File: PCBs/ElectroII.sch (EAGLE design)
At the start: 30 parts, among them J1 U.FL-R-SMT(01), U1 RFM95W-868S2, U2 TPS61090RSAR

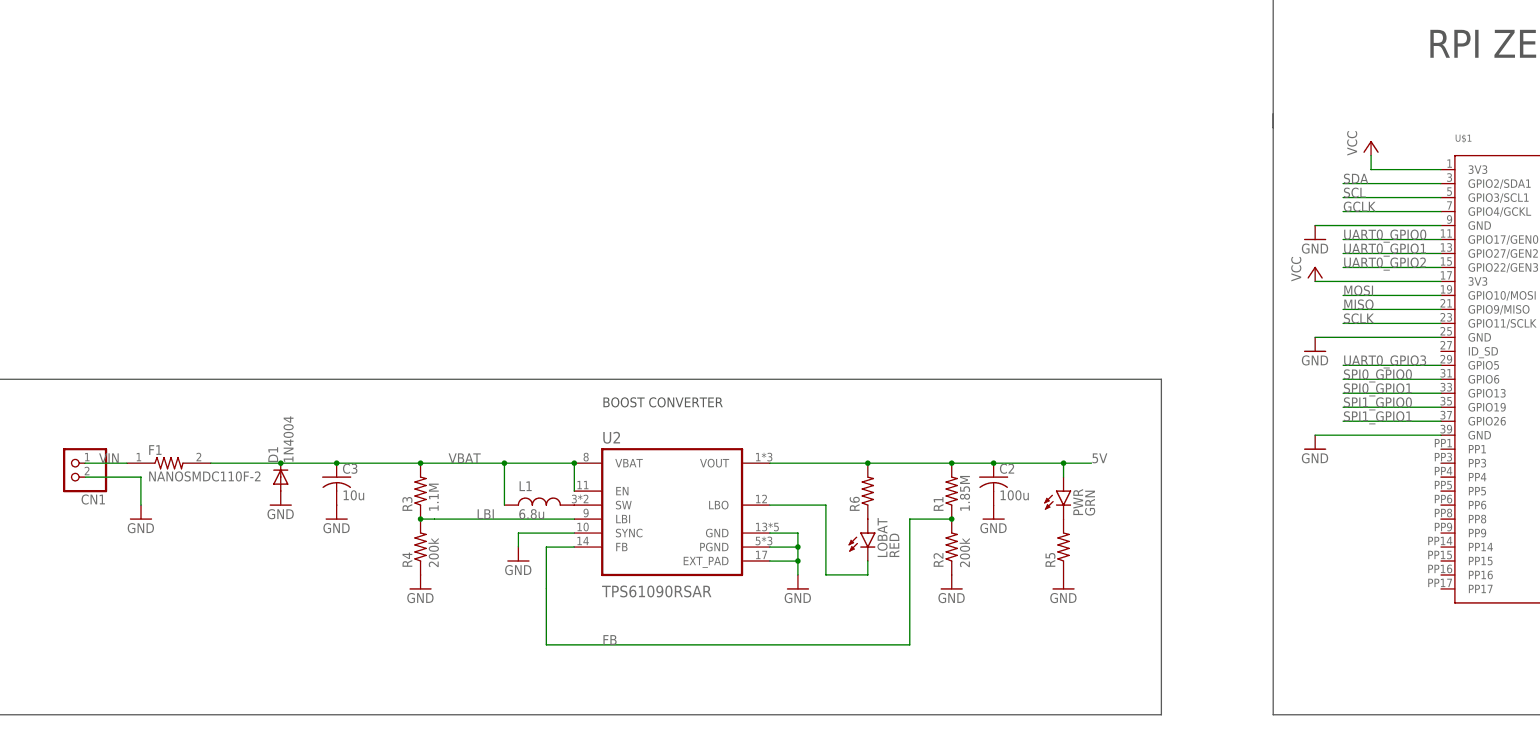
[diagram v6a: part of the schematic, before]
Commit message: Added sample pins and new trace ideas
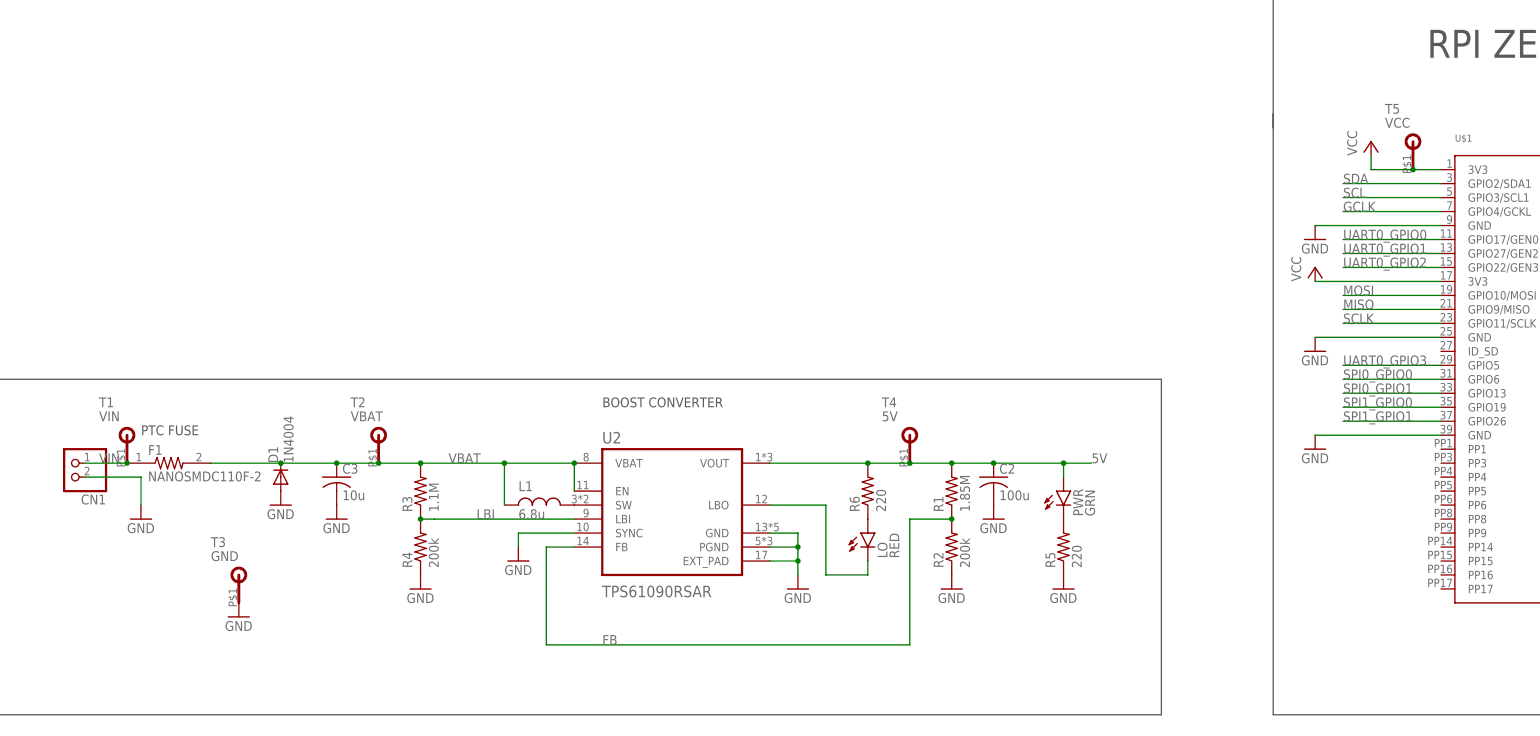
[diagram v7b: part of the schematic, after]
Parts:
- added T1: VIN, RTR Main Library:TEST_PAD
- added T2: VBAT, RTR Main Library:TEST_PAD
- added T3: GND, RTR Main Library:TEST_PAD
- added T4: 5V, RTR Main Library:TEST_PAD
- added T5: VCC, RTR Main Library:TEST_PAD
- R5, R6: value (none) -> 220
- renumbered LOBAT to LO
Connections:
- net 5V: now also T4.P$1
- net GND: now also T3.P$1
- net VBAT: now also T2.P$1
- net VCC: now also T5.P$1
- net VIN: now also T1.P$1
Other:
- note added: "PTC FUSE"
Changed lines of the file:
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@@
 </class>
 <class number="1" name="PWR" width="0.508" drill="0">
-<clearance class="1" value="0.1524"/>
+<clearance class="1" value="0.2032"/>
 </class>
 <class number="2" name="GND" width="0.508" drill="0">
-<clearance class="2" value="0.1524"/>
+<clearance class="2" value="0.2032"/>
+</class>
+<class number="3" name="ANT" width="0.2032" drill="0">
+<clearance class="3" value="0.3048"/>
 </class>
 </classes>
@@
 <part name="R4" library="RTR Main Library" deviceset="R-ALL_PACKAGES" device="R1206" value="200k"/>
 <part name="PWR" library="RTR Main Library" deviceset="LED" device="5MM" package3d_urn="urn:adsk.eagle:package:15799/2" value="GRN"/>
-<part name="R5" library="RTR Main Library" deviceset="R-ALL_PACKAGES" device="R1206"/>
+<part name="R5" library="RTR Main Library" deviceset="R-ALL_PACKAGES" device="R1206" value="220"/>
 <part name="GND22" library="RTR Main Library" deviceset="GND" device=""/>
 <part name="C3" library="RTR Main Library" deviceset="C-ALL_PACKAGES" device="C1206" value="10u"/>
 <part name="GND23" library="RTR Main Library" deviceset="GND" device=""/>
-<part name="LOBAT" library="RTR Main Library" deviceset="LED" device="5MM" package3d_urn="urn:adsk.eagle:package:15799/2" value="RED"/>
-<part name="R6" library="RTR Main Library" deviceset="R-ALL_PACKAGES" device="R1206"/>
+<part name="LO" library="RTR Main Library" deviceset="LED" device="5MM" package3d_urn="urn:adsk.eagle:package:15799/2" value="RED"/>
+<part name="R6" library="RTR Main Library" deviceset="R-ALL_PACKAGES" device="R1206" value="220"/>
 <part name="D1" library="adafruit" library_urn="urn:adsk.eagle:library:420" deviceset="1N4004" device="" package3d_urn="urn:adsk.eagle:package:6240344/1"/>
 <part name="GND24" library="RTR Main Library" deviceset="GND" device=""/>
@@
 <part name="GND25" library="RTR Main Library" deviceset="GND" device=""/>
 <part name="F1" library="NANOSMDC110F-2" deviceset="NANOSMDC110F-2" device=""/>
+<part name="GND26" library="RTR Main Library" deviceset="GND" device=""/>
+<part name="T1" library="RTR Main Library" deviceset="TEST_PAD" device="" value="VIN"/>
+<part name="T2" library="RTR Main Library" deviceset="TEST_PAD" device="" value="VBAT"/>
+<part name="T3" library="RTR Main Library" deviceset="TEST_PAD" device="" value="GND"/>
+<part name="T4" library="RTR Main Library" deviceset="TEST_PAD" device="" value="5V"/>
+<part name="T5" library="RTR Main Library" deviceset="TEST_PAD" device="" value="VCC"/>
 </parts>
 <sheets>
@@
 <wire x1="-322.58" y1="-68.58" x2="-322.58" y2="-7.62" width="0.1524" layer="97"/>
 <text x="-175.26" y="-12.7" size="1.778" layer="97">BOOST CONVERTER</text>
+<text x="-259.08" y="-17.78" size="1.778" layer="97">PTC FUSE</text>
 </plain>
 <instances>
@@
 <attribute name="VALUE" x="-226.06" y="-35.56" size="1.778" layer="96"/>
 </instance>
-<instance part="LOBAT" gate="G$1" x="-127" y="-35.56" smashed="yes">
+<instance part="LO" gate="G$1" x="-127" y="-35.56" smashed="yes">
 <attribute name="NAME" x="-123.444" y="-40.132" size="1.778" layer="95" rot="R90"/>
 <attribute name="VALUE" x="-121.285" y="-40.132" size="1.778" layer="96" rot="R90"/>
@@
 <attribute name="NAME" x="-257.81" y="-21.3614" size="1.778" layer="95"/>
 <attribute name="VALUE" x="-257.81" y="-26.162" size="1.778" layer="96"/>
+</instance>
+<instance part="GND26" gate="1" x="-241.3" y="-50.8" smashed="yes">
+<attribute name="VALUE" x="-243.84" y="-53.34" size="1.778" layer="96"/>
+</instance>
+<instance part="T1" gate="G$1" x="-261.62" y="-20.32" smashed="yes">
+<attribute name="NAME" x="-266.7" y="-12.7" size="1.778" layer="95"/>
+<attribute name="VALUE" x="-266.7" y="-15.24" size="1.778" layer="96"/>
+</instance>
+<instance part="T2" gate="G$1" x="-215.9" y="-20.32" smashed="yes">
+<attribute name="NAME" x="-220.98" y="-12.7" size="1.778" layer="95"/>
+<attribute name="VALUE" x="-220.98" y="-15.24" size="1.778" layer="96"/>
+</instance>
+<instance part="T3" gate="G$1" x="-241.3" y="-45.72" smashed="yes">
+<attribute name="NAME" x="-246.38" y="-38.1" size="1.778" layer="95"/>
+<attribute name="VALUE" x="-246.38" y="-40.64" size="1.778" layer="96"/>
+</instance>
+<instance part="T4" gate="G$1" x="-119.38" y="-20.32" smashed="yes">
+<attribute name="NAME" x="-124.46" y="-12.7" size="1.778" layer="95"/>
+<attribute name="VALUE" x="-124.46" y="-15.24" size="1.778" layer="96"/>
+</instance>
+<instance part="T5" gate="G$1" x="-27.94" y="33.02" smashed="yes">
+<attribute name="NAME" x="-33.02" y="40.64" size="1.778" layer="95"/>
+<attribute name="VALUE" x="-33.02" y="38.1" size="1.778" layer="96"/>
 </instance>
 </instances>
@@
 <pinref part="U2" gate="G$1" pin="VOUT"/>
 <wire x1="-144.78" y1="-22.86" x2="-127" y2="-22.86" width="0.1524" layer="91"/>
-<wire x1="-127" y1="-22.86" x2="-111.76" y2="-22.86" width="0.1524" layer="91"/>
+<wire x1="-127" y1="-22.86" x2="-119.38" y2="-22.86" width="0.1524" layer="91"/>
+<wire x1="-119.38" y1="-22.86" x2="-111.76" y2="-22.86" width="0.1524" layer="91"/>
 <wire x1="-111.76" y1="-22.86" x2="-104.14" y2="-22.86" width="0.1524" layer="91"/>
 <junction x="-111.76" y="-22.86"/>
@@
 <junction x="-127" y="-22.86"/>
 <label x="-86.36" y="-22.86" size="1.778" layer="95"/>
+<junction x="-119.38" y="-22.86"/>
+<pinref part="T4" gate="G$1" pin="P$1"/>
 </segment>
 </net>
@@
 <wire x1="-259.08" y1="-25.4" x2="-259.08" y2="-30.48" width="0.1524" layer="91"/>
 </segment>
+<segment>
+<pinref part="GND26" gate="1" pin="GND"/>
+<pinref part="T3" gate="G$1" pin="P$1"/>
+</segment>
 </net>
 <net name="MOSI" class="0">
@@
 </segment>
 <segment>
-<wire x1="-22.86" y1="30.48" x2="-35.56" y2="30.48" width="0.1524" layer="91"/>
+<wire x1="-22.86" y1="30.48" x2="-27.94" y2="30.48" width="0.1524" layer="91"/>
 <pinref part="P+6" gate="VCC" pin="VCC"/>
+<wire x1="-27.94" y1="30.48" x2="-35.56" y2="30.48" width="0.1524" layer="91"/>
 <wire x1="-35.56" y1="30.48" x2="-35.56" y2="33.02" width="0.1524" layer="91"/>
 <pinref part="U$1" gate="G$1" pin="3V3@1"/>
+<pinref part="T5" gate="G$1" pin="P$1"/>
+<junction x="-27.94" y="30.48"/>
 </segment>
 <segment>
@@
 </segment>
 </net>
-<net name="ANT" class="0">
+<net name="ANT" class="3">
 <segment>
 <pinref part="U1" gate="G$1" pin="ANT"/>
@@
 <label x="-203.2" y="-22.86" size="1.778" layer="95"/>
 <pinref part="C3" gate="G$1" pin="1"/>
-<wire x1="-208.28" y1="-22.86" x2="-223.52" y2="-22.86" width="0.1524" layer="91"/>
+<wire x1="-208.28" y1="-22.86" x2="-215.9" y2="-22.86" width="0.1524" layer="91"/>
 <junction x="-180.34" y="-22.86"/>
 <pinref part="U2" gate="G$1" pin="EN"/>
+<wire x1="-215.9" y1="-22.86" x2="-223.52" y2="-22.86" width="0.1524" layer="91"/>
 <wire x1="-180.34" y1="-22.86" x2="-180.34" y2="-27.94" width="0.1524" layer="91"/>
 <junction x="-223.52" y="-22.86"/>
@@
 <wire x1="-233.68" y1="-22.86" x2="-246.38" y2="-22.86" width="0.1524" layer="91"/>
 <pinref part="F1" gate="G$1" pin="2"/>
+<junction x="-215.9" y="-22.86"/>
+<pinref part="T2" gate="G$1" pin="P$1"/>
 </segment>
 </net>
@@
 <segment>
 <pinref part="R6" gate="G$1" pin="1"/>
-<pinref part="LOBAT" gate="G$1" pin="A"/>
+<pinref part="LO" gate="G$1" pin="A"/>
 </segment>
 </net>
@@
 <wire x1="-134.62" y1="-30.48" x2="-134.62" y2="-43.18" width="0.1524" layer="91"/>
 <wire x1="-134.62" y1="-43.18" x2="-127" y2="-43.18" width="0.1524" layer="91"/>
-<pinref part="LOBAT" gate="G$1" pin="C"/>
+<pinref part="LO" gate="G$1" pin="C"/>
 <wire x1="-127" y1="-43.18" x2="-127" y2="-40.64" width="0.1524" layer="91"/>
 </segment>
@@
 <label x="-266.7" y="-22.86" size="1.778" layer="95"/>
 <pinref part="F1" gate="G$1" pin="1"/>
-</segment>
-</net>
+<pinref part="T1" gate="G$1" pin="P$1"/>
+<junction x="-261.62" y="-22.86"/>
+</segment>
+</net>
